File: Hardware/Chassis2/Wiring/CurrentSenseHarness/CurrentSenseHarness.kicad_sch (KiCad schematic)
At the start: 11 parts, among them J1 0022011042, J2 0022011042

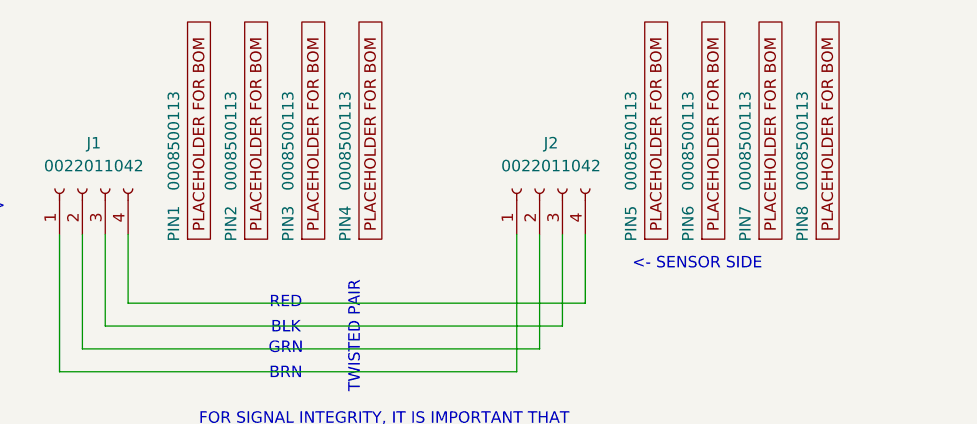
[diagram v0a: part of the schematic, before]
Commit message: Update GDVS and current sense harness schematics
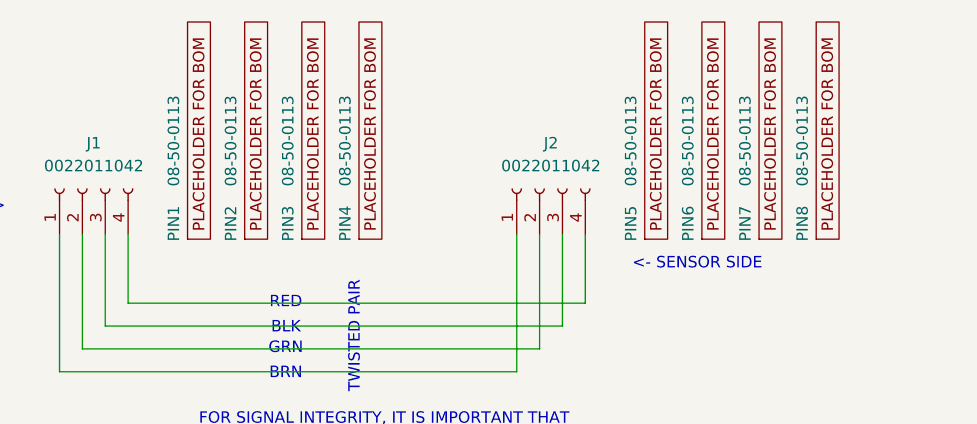
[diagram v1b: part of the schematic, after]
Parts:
- PIN1, PIN2, PIN3, PIN4, PIN5, PIN6, PIN7, PIN8: value 0008500113 -> 08-50-0113
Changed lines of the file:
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@@
 			)
 		)
-		(property "Value" "0008500113"
+		(property "Value" "08-50-0113"
 			(at 114.3 27.686 0)
 			(show_name no)
@@
 			)
 		)
-		(property "Value" "0008500113"
+		(property "Value" "08-50-0113"
 			(at 158.75 27.686 0)
 			(show_name no)
@@
 			)
 		)
-		(property "Value" "0008500113"
+		(property "Value" "08-50-0113"
 			(at 120.65 27.686 0)
 			(show_name no)
@@
 			)
 		)
-		(property "Value" "0008500113"
+		(property "Value" "08-50-0113"
 			(at 152.4 27.686 0)
 			(show_name no)
@@
 			)
 		)
-		(property "Value" "0008500113"
+		(property "Value" "08-50-0113"
 			(at 171.45 27.686 0)
 			(show_name no)
@@
 			)
 		)
-		(property "Value" "0008500113"
+		(property "Value" "08-50-0113"
 			(at 165.1 27.686 0)
 			(show_name no)
@@
 			)
 		)
-		(property "Value" "0008500113"
+		(property "Value" "08-50-0113"
 			(at 107.95 27.686 0)
 			(show_name no)
@@
 			)
 		)
-		(property "Value" "0008500113"
+		(property "Value" "08-50-0113"
 			(at 101.6 27.686 0)
 			(show_name no)

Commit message: Rename Open Inverter Platform to InverterGen5, schematic PDF export, tidy variants
- Title blocks renamed to InverterGen5 in all harness schematics
- regen now re-exports schematic PDFs for boards and harnesses too
- Spares variants live under FabricationData/BOMs/Variants/
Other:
- title: Open Inverter Platform - Current Sensor Wiring Harness -> InverterGen5 - Current Sensor Wiring Harness
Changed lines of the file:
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@@
 	(paper "USLetter")
 	(title_block
-		(title "Open Inverter Platform - Current Sensor Wiring Harness")
+		(title "InverterGen5 - Current Sensor Wiring Harness")
 		(date "2026-07-16")
 		(rev "A")
